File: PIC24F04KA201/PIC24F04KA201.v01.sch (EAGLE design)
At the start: 23 parts, among them IC2 3V3-APE1117K-33-HF-3, IC3 3V3-APE1117K-33-HF-3

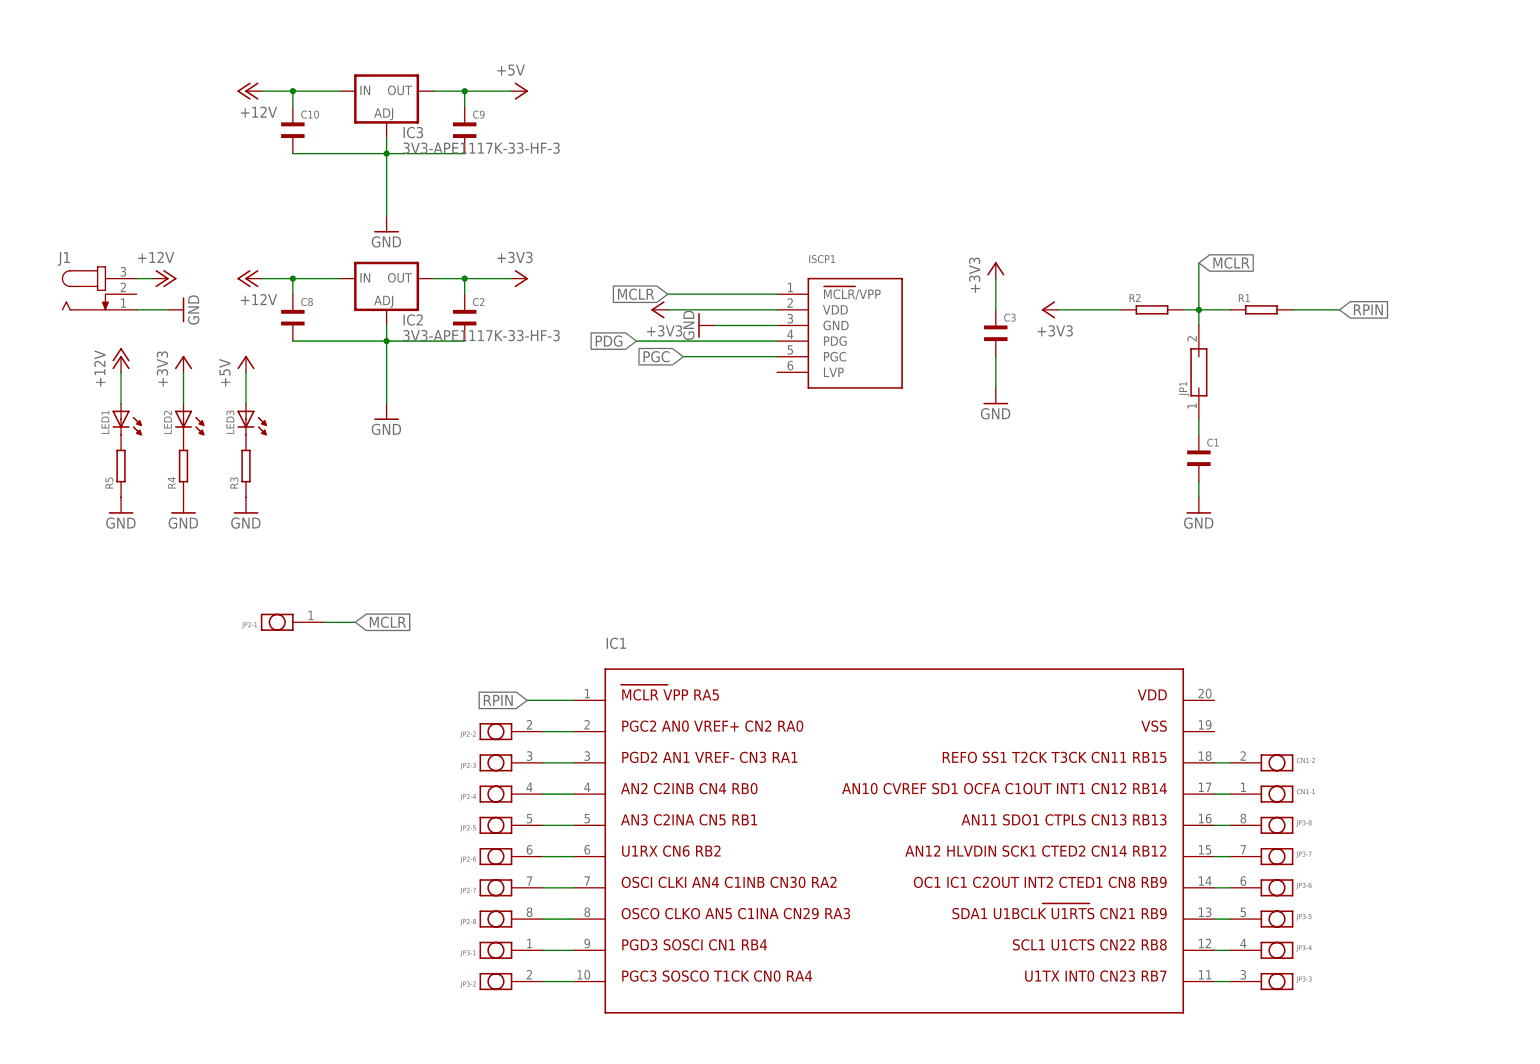
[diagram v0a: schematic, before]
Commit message: Update - added jumpers & Vreg's
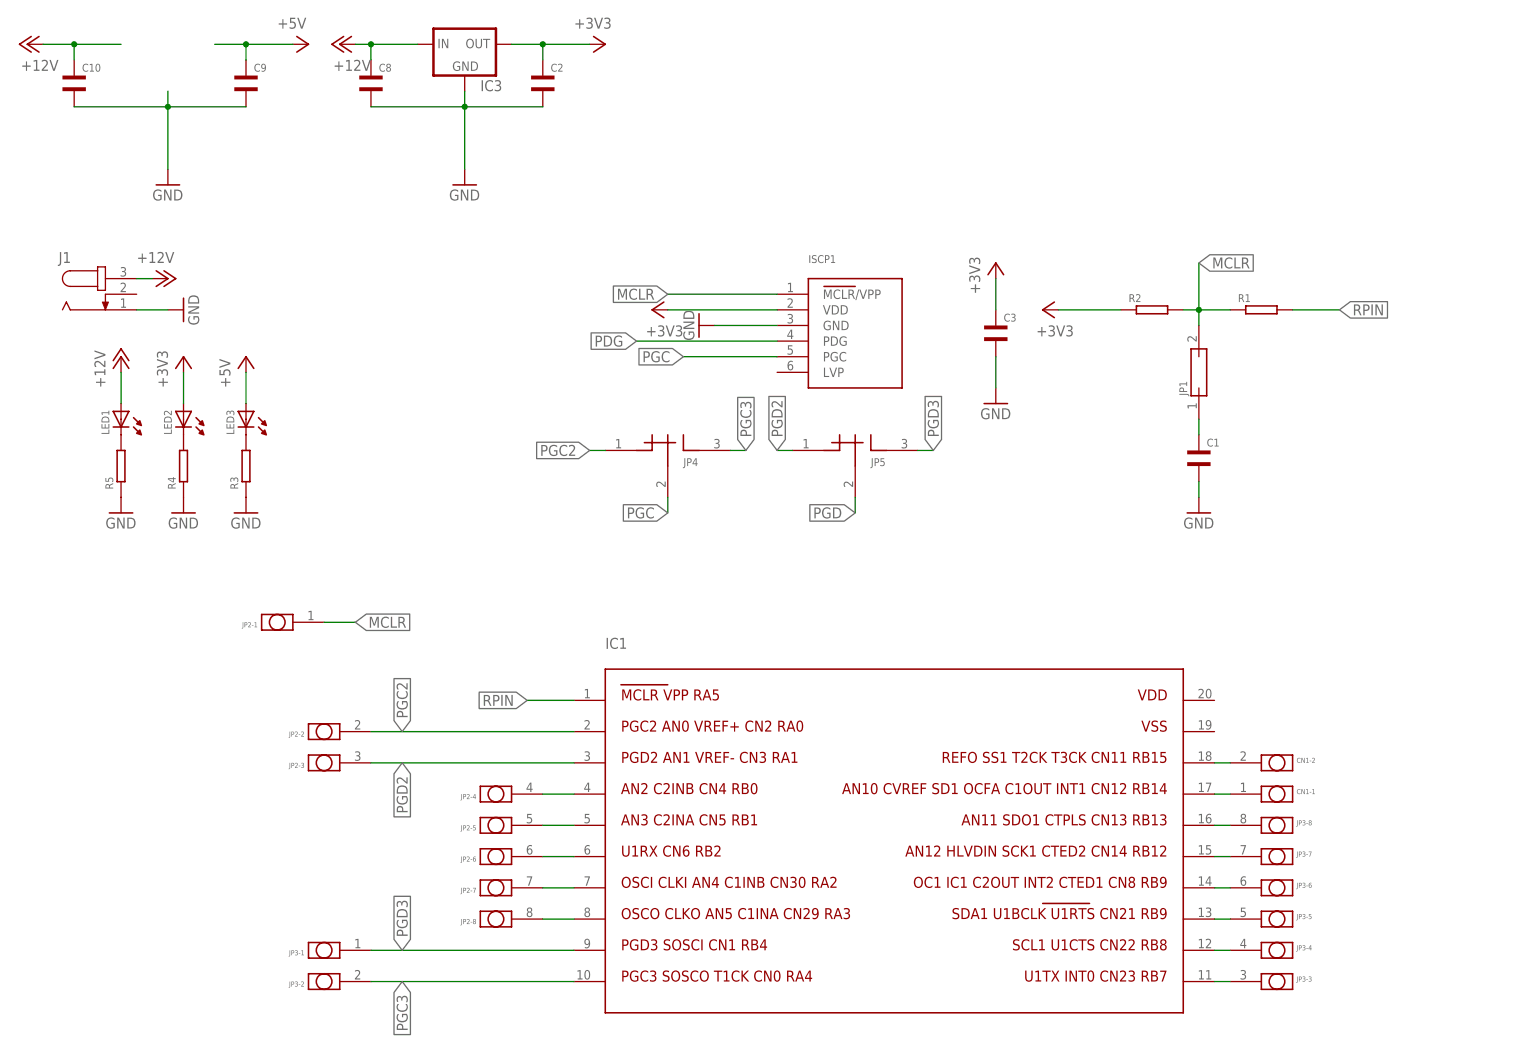
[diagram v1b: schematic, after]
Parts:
- removed IC2: 3V3-APE1117K-33-HF-3, SM-VReg:3V3-APE1117K-33-HF-3
- added JP4, JP5: (no value), SM-Jumper:JP-OR
- IC3: value 3V3-APE1117K-33-HF-3 -> (none); device SM-VReg:3V3-APE1117K-33-HF-3 -> SM-VReg:LD1117V33
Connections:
- removed net N$2: IC1.P$2, JP2-2.P$1
- removed net N$20: IC1.P$9, JP3-1.P$1
- removed net N$21: IC1.P$10, JP3-2.P$1
- removed net N$3: IC1.P$3, JP2-3.P$1
- new net PGC2: IC1.P$2, JP2-2.P$1, JP4.P$1
- new net PGC3: IC1.P$10, JP3-2.P$1, JP4.P$2
- new net PGD: JP5.P$3
- new net PGD2: IC1.P$3, JP2-3.P$1, JP5.P$1
- new net PGD3: IC1.P$9, JP3-1.P$1, JP5.P$2
- net +12V: no longer IC2.IN
- net +3V3: now also IC3.OUT; no longer IC2.OUT
- net +5V: no longer IC3.OUT
- net GND: now also IC3.GND; no longer IC2.ADJ, IC3.ADJ
- net PGC: now also JP4.P$3
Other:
- moved on the sheet: C10, C2, C8, C9, IC3, JP2-2, JP2-3, JP3-1, JP3-2

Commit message: Small parts update
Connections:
- removed net PGD: JP5.P$3
- net PDG: now also JP5.P$3
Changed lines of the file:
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@@
 <label x="-40.64" y="78.74" size="1.778" layer="95" rot="R180" xref="yes"/>
+</segment>
+<segment>
+<pinref part="JP5" gate="G$1" pin="P$3"/>
+<wire x1="-5.08" y1="53.34" x2="-5.08" y2="50.8" width="0.1524" layer="91"/>
+<label x="-5.08" y="50.8" size="1.778" layer="95" rot="R180" xref="yes"/>
 </segment>
 </net>
@@
 </segment>
 </net>
-<net name="PGD" class="0">
-<segment>
-<pinref part="JP5" gate="G$1" pin="P$3"/>
-<wire x1="-5.08" y1="53.34" x2="-5.08" y2="50.8" width="0.1524" layer="91"/>
-<label x="-5.08" y="50.8" size="1.778" layer="95" rot="R180" xref="yes"/>
-</segment>
-</net>

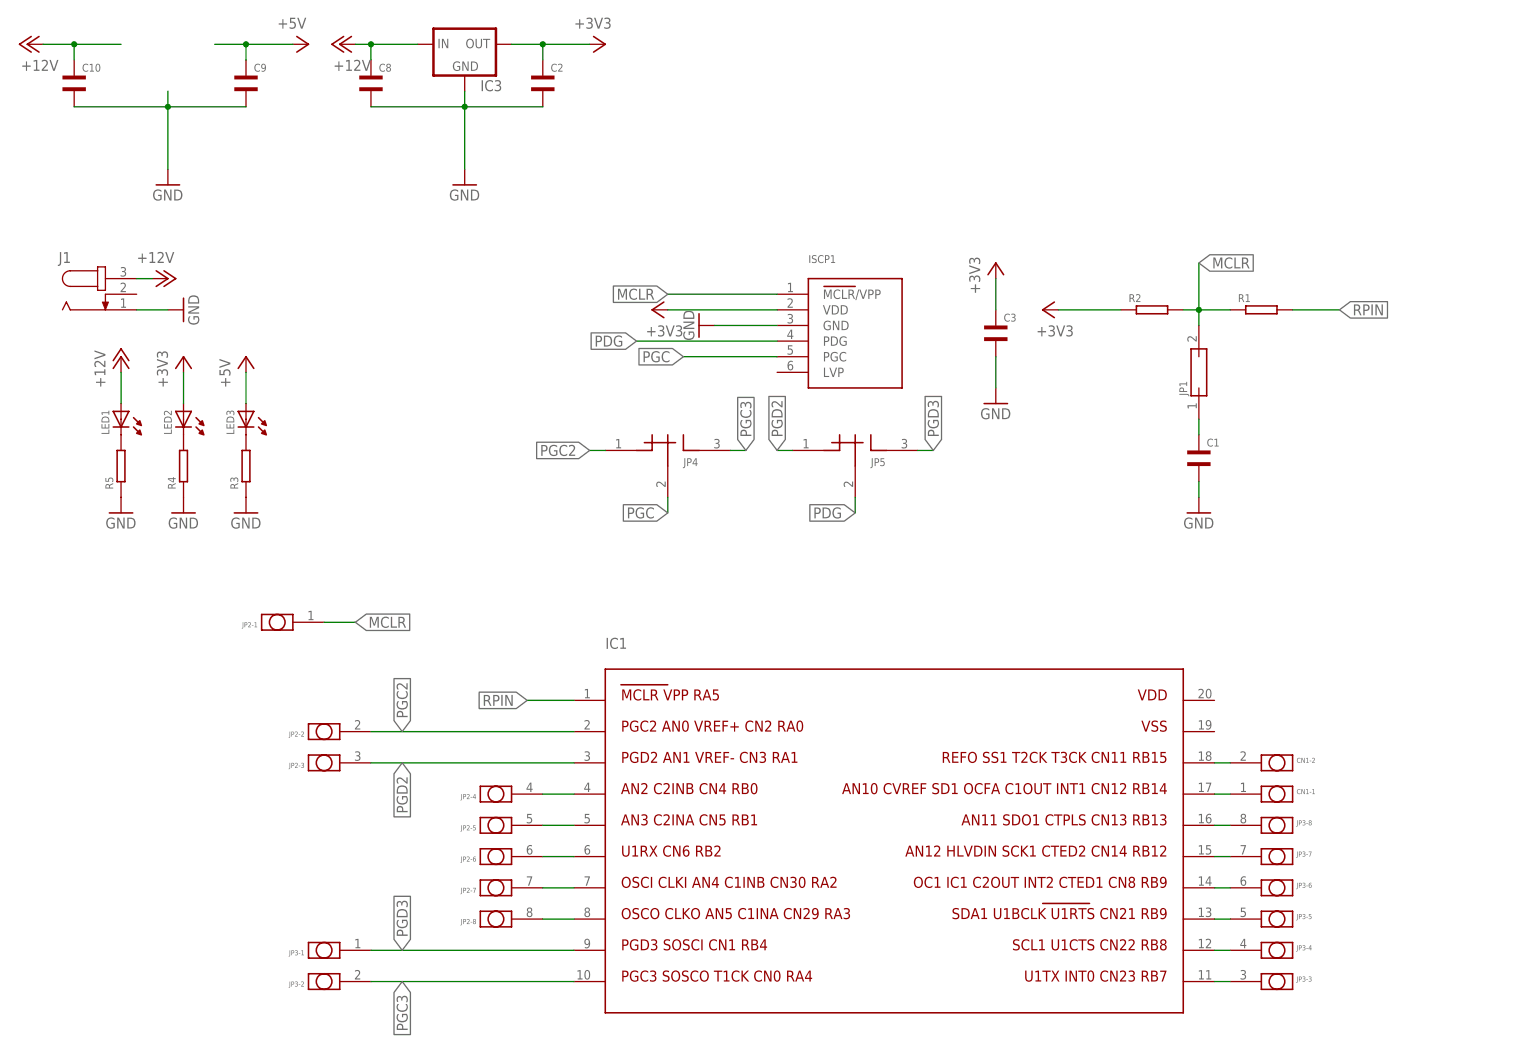
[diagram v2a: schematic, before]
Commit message: Added correct values for resistors, resynced the board file
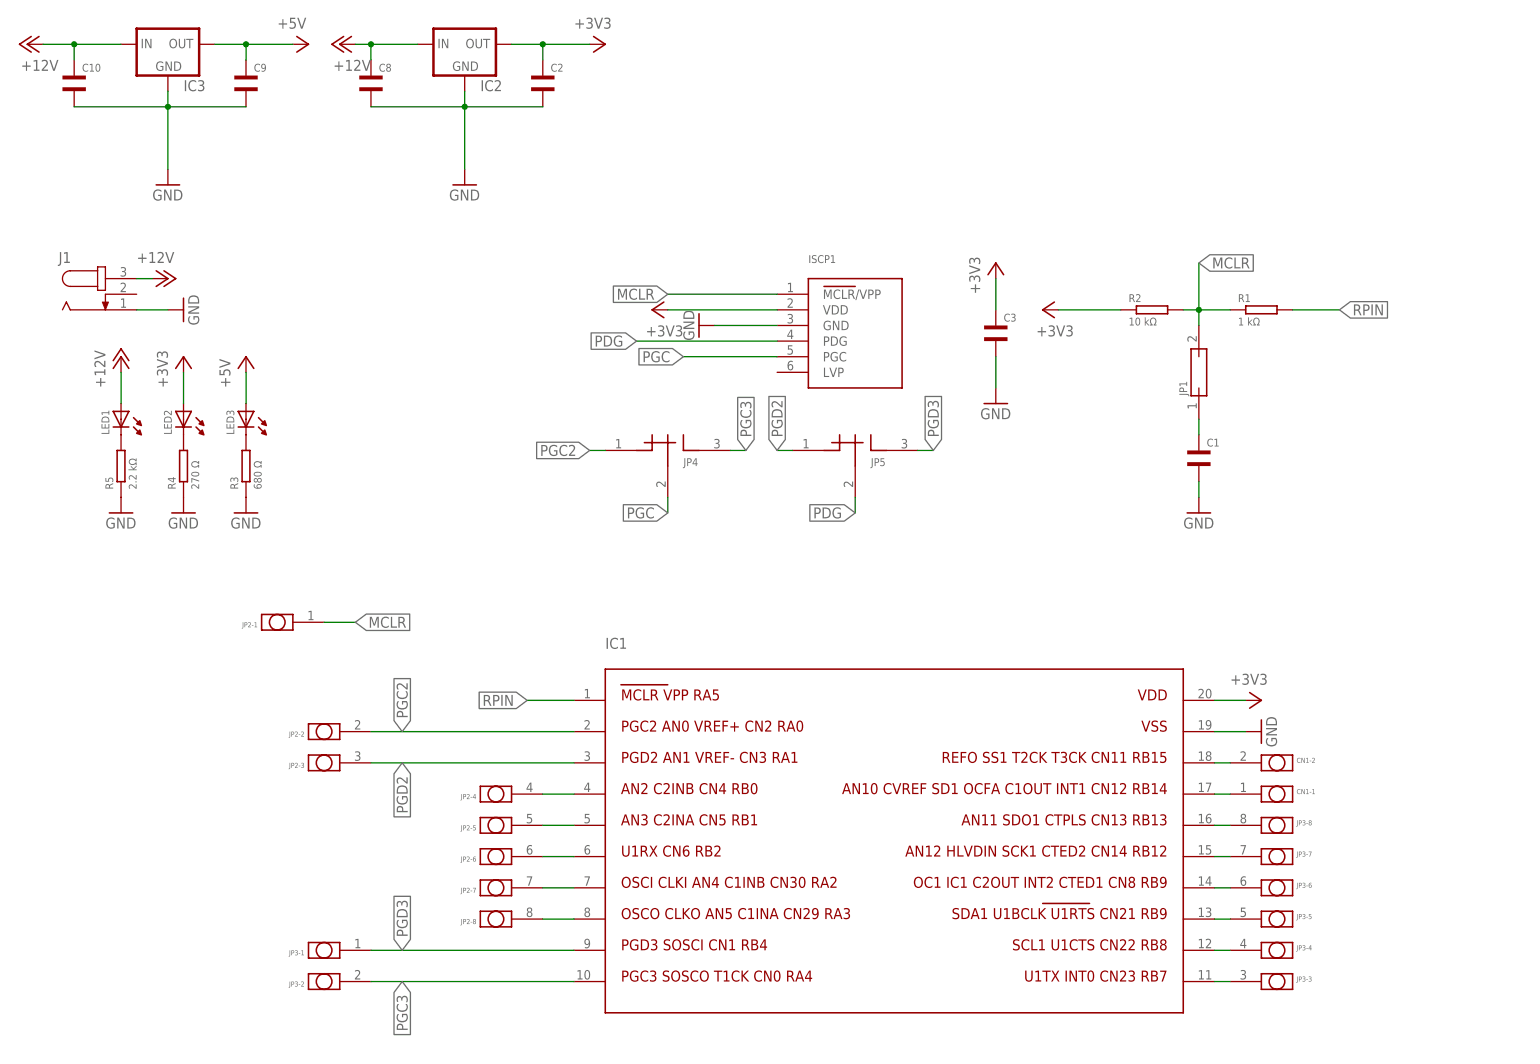
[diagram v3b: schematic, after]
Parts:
- added IC2: (no value), SM-VReg:LD1117V33
- IC3: device SM-VReg:LD1117V33 -> SM-VReg:L78S05CV
- R1: value (none) -> 1 kΩ; device SM-Resistor:RESITOR-SMD-0805 -> SM-Resistor:CRCW08051K00FKTABC
- R2: value (none) -> 10 kΩ; device SM-Resistor:RESITOR-SMD-0805 -> SM-Resistor:CRCW080510K0FKTABC
- R3: value (none) -> 680 Ω; device SM-Resistor:RESITOR-SMD-0805 -> SM-Resistor:CRCW0805680RFKTABC
- R4: value (none) -> 270 Ω; device SM-Resistor:RESITOR-SMD-0805 -> SM-Resistor:CRCW0805270RFKTABC
- R5: value (none) -> 2.2 kΩ; device SM-Resistor:RESITOR-SMD-0805 -> SM-Resistor:CRCW08052K20FKTABC
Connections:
- net +12V: now also IC2.IN
- net +3V3: now also IC1.P$20, IC2.OUT; no longer IC3.OUT
- net +5V: now also IC3.OUT
- net GND: now also IC1.P$19, IC2.GND
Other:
- moved on the sheet: IC3
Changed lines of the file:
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@@
 <parts>
 <part name="IC1" library="SM-Microchip" deviceset="PIC24F04KA201" device=""/>
-<part name="R1" library="SM-Resistor" deviceset="RESITOR" device="-SMD-0805"/>
-<part name="R2" library="SM-Resistor" deviceset="RESITOR" device="-SMD-0805"/>
+<part name="R1" library="SM-Resistor" deviceset="CRCW0805" device="1K00FKTABC" value="1 kΩ"/>
+<part name="R2" library="SM-Resistor" deviceset="CRCW0805" device="10K0FKTABC" value="10 kΩ"/>
 <part name="+3V1" library="supply1" deviceset="+3V3" device=""/>
 <part name="GND1" library="supply1" deviceset="GND" device=""/>
@@
 <part name="LED2" library="SM-LED" deviceset="LED" device="-SMD-0805"/>
 <part name="LED3" library="SM-LED" deviceset="LED" device="-SMD-0805"/>
-<part name="R3" library="SM-Resistor" deviceset="RESITOR" device="-SMD-0805"/>
-<part name="R4" library="SM-Resistor" deviceset="RESITOR" device="-SMD-0805"/>
-<part name="R5" library="SM-Resistor" deviceset="RESITOR" device="-SMD-0805"/>
+<part name="R3" library="SM-Resistor" deviceset="CRCW0805" device="680RFKTABC" value="680 Ω"/>
+<part name="R4" library="SM-Resistor" deviceset="CRCW0805" device="270RFKTABC" value="270 Ω"/>
+<part name="R5" library="SM-Resistor" deviceset="CRCW0805" device="2K20FKTABC" value="2.2 kΩ"/>
 <part name="GND6" library="supply1" deviceset="GND" device=""/>
 <part name="GND7" library="supply1" deviceset="GND" device=""/>
@@
 <part name="JP3" library="SM-PinHeader" deviceset="1X8" device=""/>
 <part name="CN1" library="SM-PinHeader" deviceset="1X2" device=""/>
-<part name="IC3" library="SM-VReg" deviceset="LD1117V33" device=""/>
 <part name="JP4" library="SM-Jumper" deviceset="JP-OR" device=""/>
 <part name="JP5" library="SM-Jumper" deviceset="JP-OR" device=""/>
+<part name="IC2" library="SM-VReg" deviceset="LD1117V33" device=""/>
+<part name="IC3" library="SM-VReg" deviceset="L78S05CV" device=""/>
+<part name="+3V6" library="supply1" deviceset="+3V3" device=""/>
+<part name="GND10" library="supply1" deviceset="GND" device=""/>
 </parts>
 <sheets>
@@
 <instance part="CN1" gate="-1" x="58.42" y="5.08"/>
 <instance part="CN1" gate="-2" x="58.42" y="10.16"/>
-<instance part="IC3" gate="G$1" x="-68.58" y="127"/>
 <instance part="JP4" gate="G$1" x="-35.56" y="60.96"/>
 <instance part="JP5" gate="G$1" x="-5.08" y="60.96"/>
+<instance part="IC2" gate="G$1" x="-68.58" y="127"/>
+<instance part="IC3" gate="G$1" x="-116.84" y="127"/>
+<instance part="+3V6" gate="G$1" x="60.96" y="20.32" rot="R270"/>
+<instance part="GND10" gate="1" x="60.96" y="15.24" rot="R90"/>
 </instances>
 <busses>
@@
 <wire x1="-55.88" y1="124.46" x2="-55.88" y2="127" width="0.1524" layer="91"/>
 <junction x="-55.88" y="127"/>
-<pinref part="IC3" gate="G$1" pin="OUT"/>
 <wire x1="-60.96" y1="127" x2="-55.88" y2="127" width="0.1524" layer="91"/>
+<pinref part="IC2" gate="G$1" pin="OUT"/>
 </segment>
 <segment>
@@
 <pinref part="+3V5" gate="G$1" pin="+3V3"/>
 <wire x1="-114.3" y1="73.66" x2="-114.3" y2="68.58" width="0.1524" layer="91"/>
+</segment>
+<segment>
+<pinref part="IC1" gate="G$1" pin="P$20"/>
+<wire x1="53.34" y1="20.32" x2="58.42" y2="20.32" width="0.1524" layer="91"/>
+<pinref part="+3V6" gate="G$1" pin="+3V3"/>
 </segment>
 </net>
@@
 <wire x1="-55.88" y1="116.84" x2="-68.58" y2="116.84" width="0.1524" layer="91"/>
 <pinref part="GND4" gate="1" pin="GND"/>
-<pinref part="IC3" gate="G$1" pin="GND"/>
+<pinref part="IC2" gate="G$1" pin="GND"/>
 </segment>
 <segment>
@@
 <wire x1="-104.14" y1="116.84" x2="-116.84" y2="116.84" width="0.1524" layer="91"/>
 <pinref part="GND9" gate="1" pin="GND"/>
+<pinref part="IC3" gate="G$1" pin="GND"/>
 </segment>
 <segment>
@@
 <pinref part="C1" gate="G$1" pin="P$1"/>
 <wire x1="50.8" y1="55.88" x2="50.8" y2="53.34" width="0.1524" layer="91"/>
+</segment>
+<segment>
+<pinref part="IC1" gate="G$1" pin="P$19"/>
+<wire x1="53.34" y1="15.24" x2="58.42" y2="15.24" width="0.1524" layer="91"/>
+<pinref part="GND10" gate="1" pin="GND"/>
 </segment>
 </net>
@@
 <junction x="-83.82" y="127"/>
 <pinref part="P+1" gate="1" pin="+12V"/>
-<pinref part="IC3" gate="G$1" pin="IN"/>
+<pinref part="IC2" gate="G$1" pin="IN"/>
 </segment>
 <segment>
@@
 <junction x="-132.08" y="127"/>
 <pinref part="P+4" gate="1" pin="+12V"/>
+<pinref part="IC3" gate="G$1" pin="IN"/>
 </segment>
 </net>
@@
 <junction x="-104.14" y="127"/>
 <pinref part="P+5" gate="1" pin="+5V"/>
-</segment>
-<segment>
+<pinref part="IC3" gate="G$1" pin="OUT"/>
+</segment>
+<segment>
